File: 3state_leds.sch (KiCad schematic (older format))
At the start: 85 parts, among them U11 74HC595, U12 74HC595, U13 74HC595, U14 74HC595, U15 74HC595

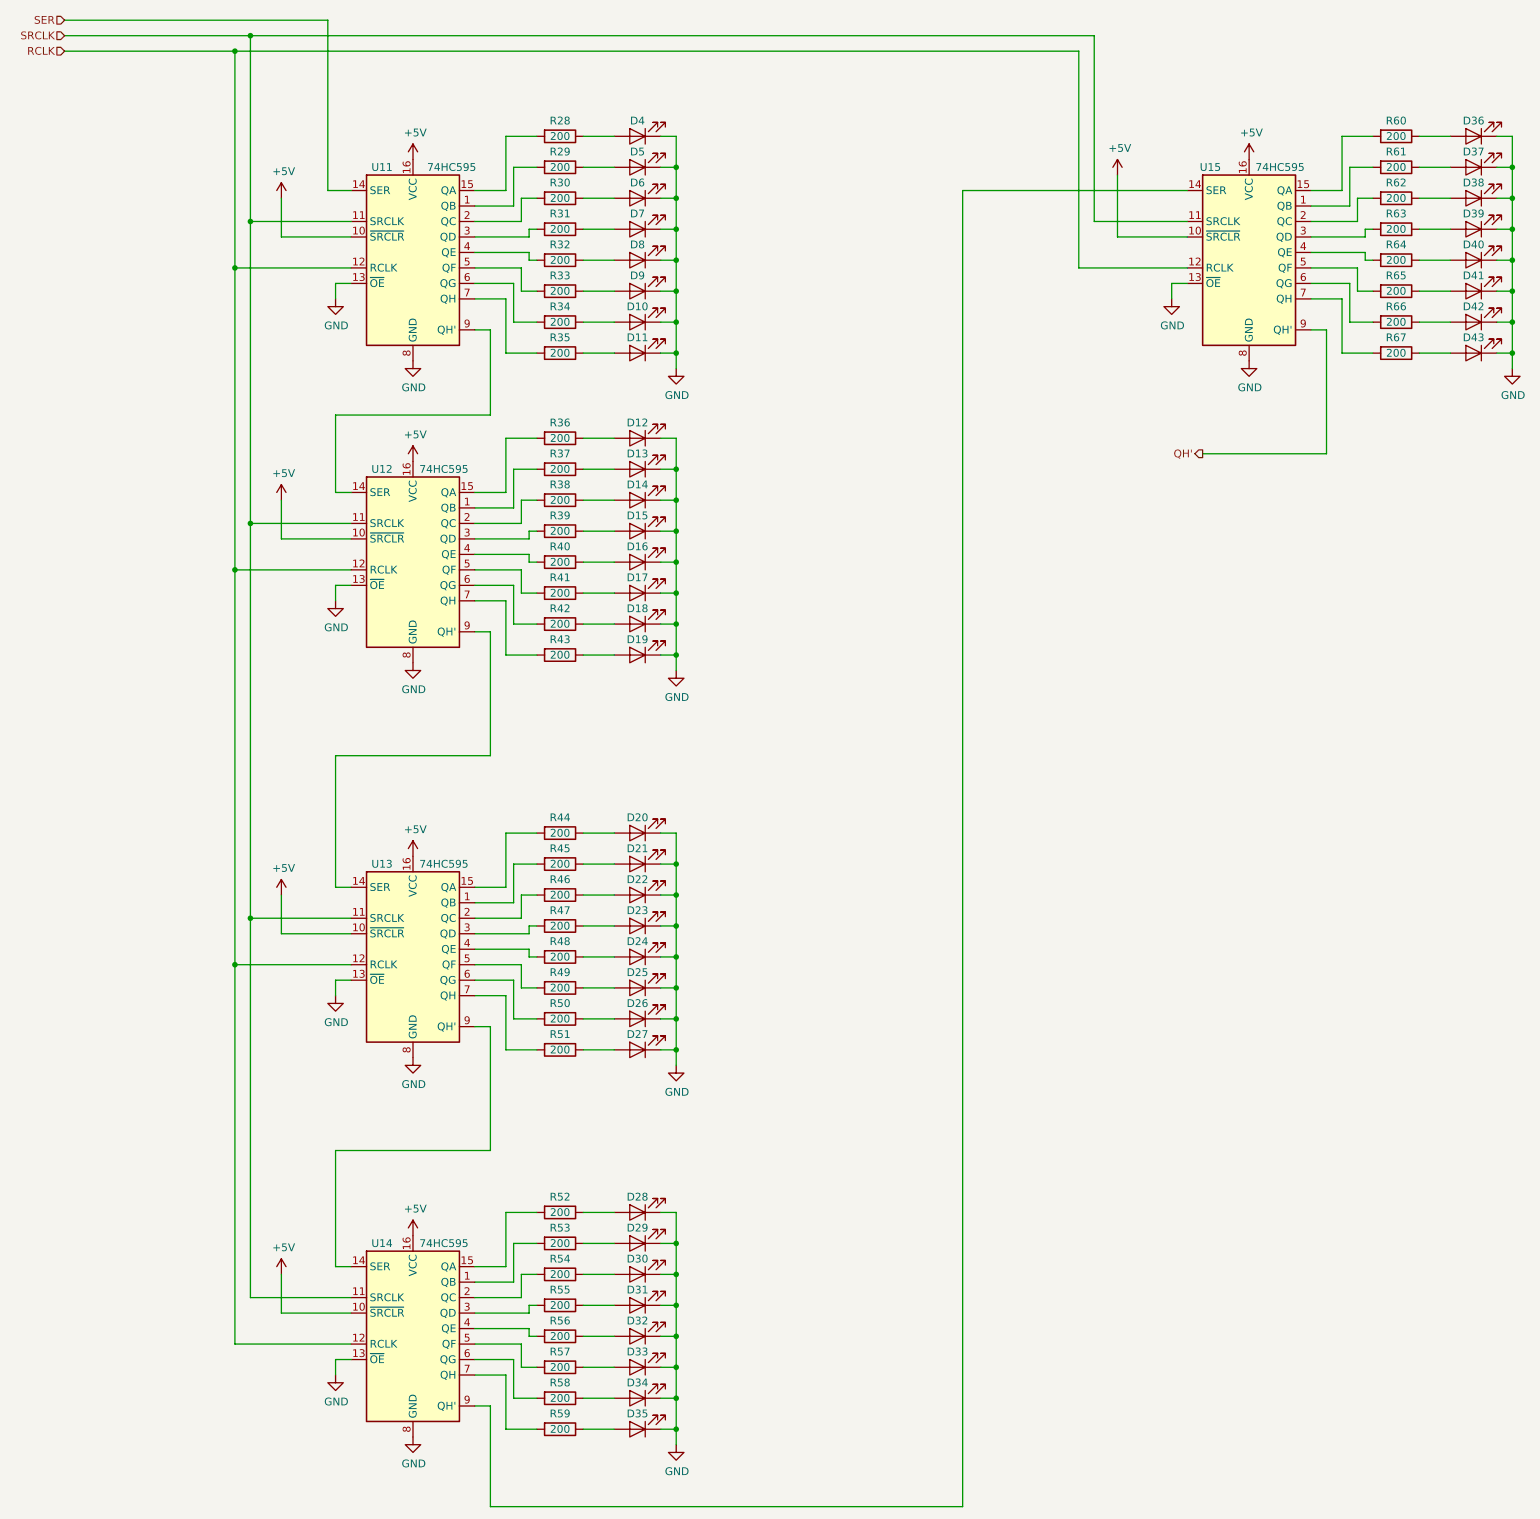
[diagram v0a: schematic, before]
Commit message: reorganized schematic; added reverse polarity protection; start adding footprints
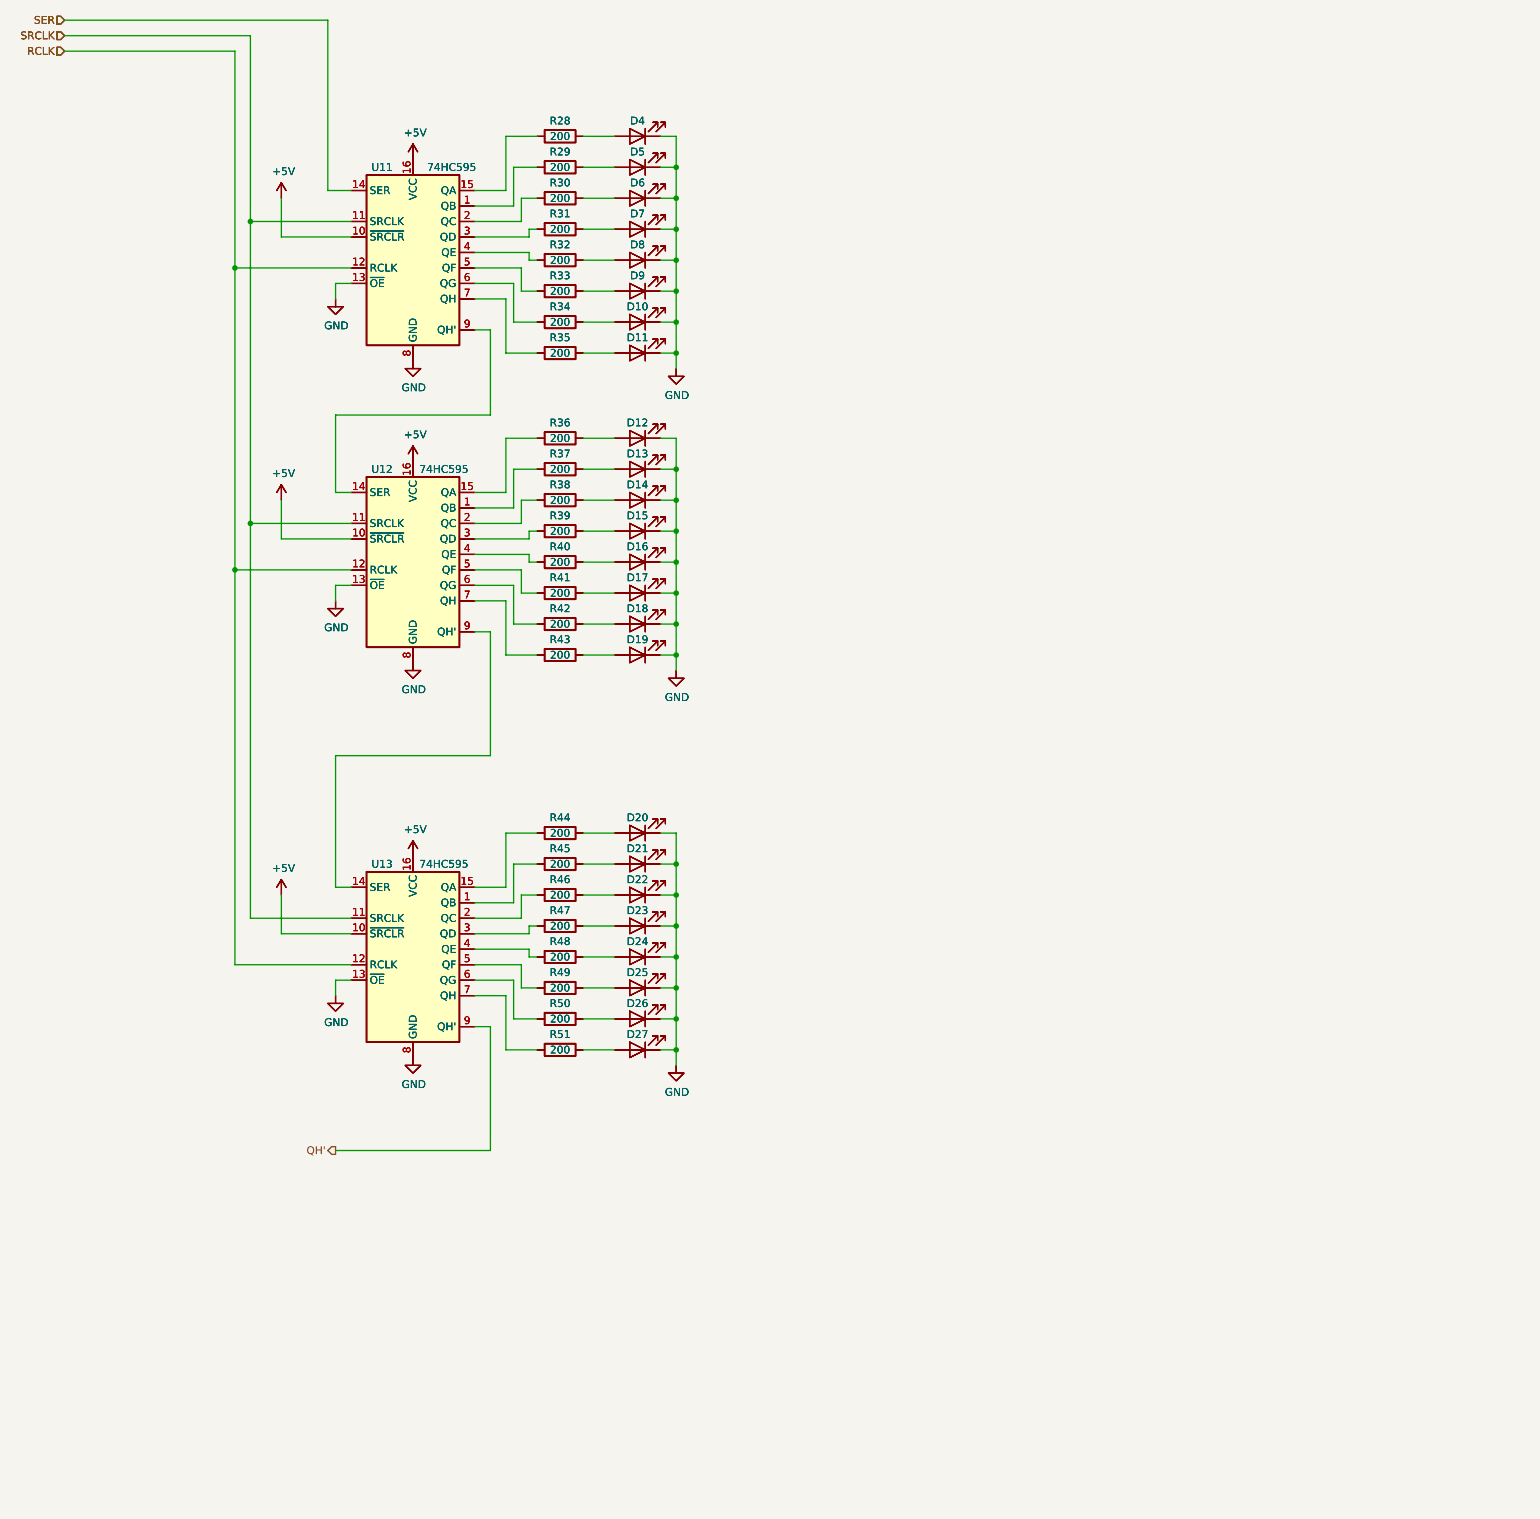
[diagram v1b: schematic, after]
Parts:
- removed D28, D29, D30, D31, D32, D33, D34, D35, D36, D37, D38, D39, D40, D41, D42, D43: LED, symbol Device:LED
- removed R52, R53, R54, R55, R56, R57, R58, R59, R60, R61, R62, R63, R64, R65, R66, R67: 200, symbol Device:R
- removed U14, U15: 74HC595, symbol 74xx:74HC595
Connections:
- net QH': now also U13.9 (QH')

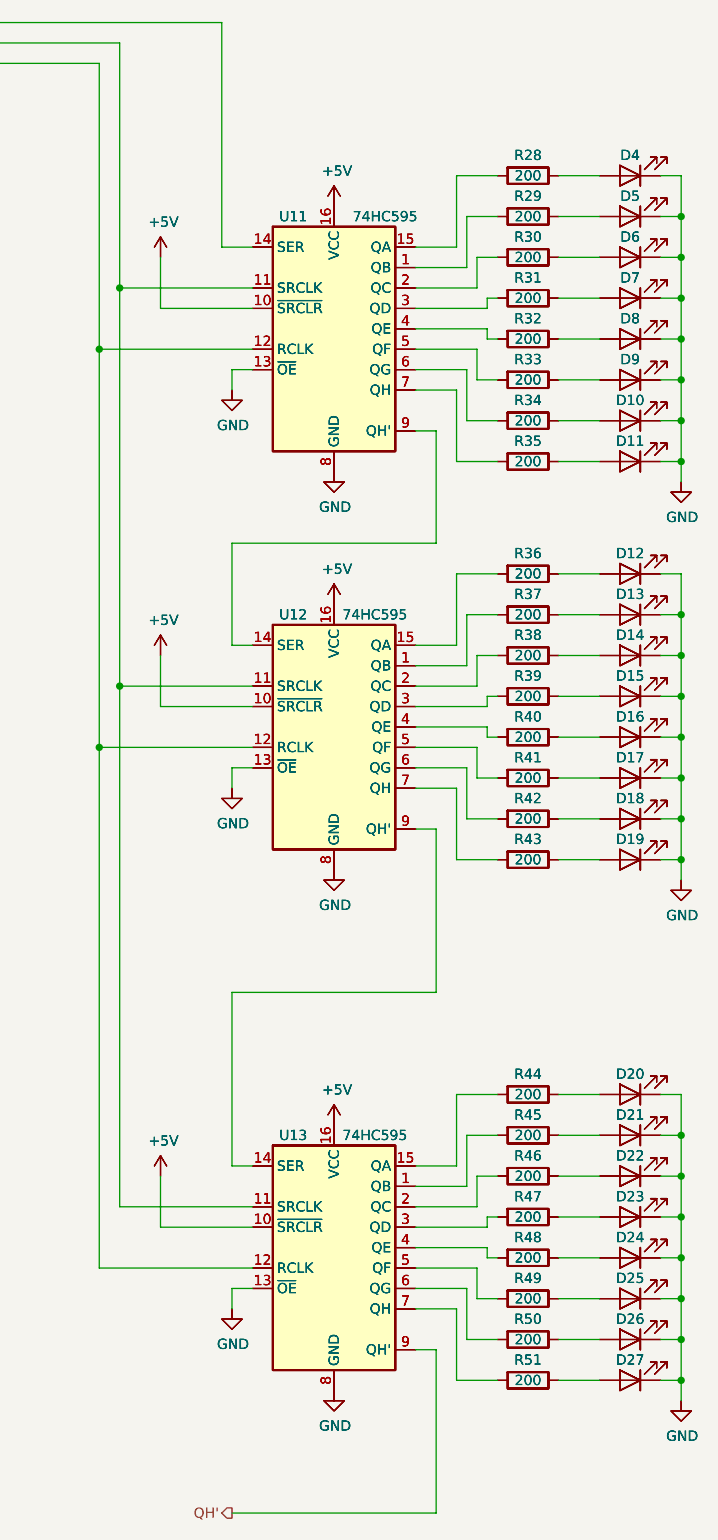
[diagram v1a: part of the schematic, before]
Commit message: footprints; library for 7seg; start pcb layout
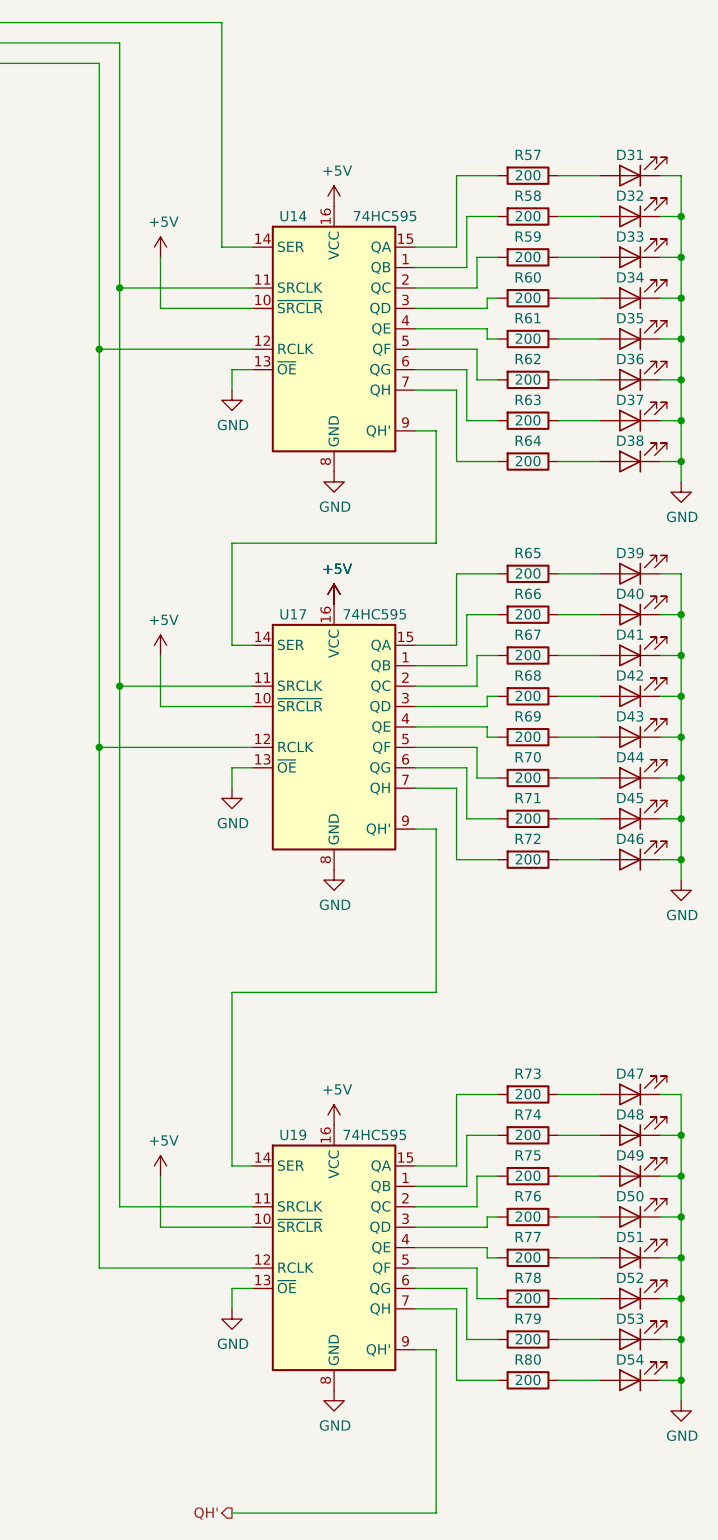
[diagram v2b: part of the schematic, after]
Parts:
- removed D10, D11, D12, D13, D14, D15, D16, D17, D18, D19, D20, D21, D22, D23, D24, D25, D26, D27, D4, D5, D6, D7, D8, D9: LED, symbol Device:LED
- removed R28, R29, R30, R31, R32, R33, R34, R35, R36, R37, R38, R39, R40, R41, R42, R43, R44, R45, R46, R47, R48, R49, R50, R51: 200, symbol Device:R
- removed U11, U12, U13: 74HC595, symbol 74xx:74HC595
- added D31, D32, D33, D34, D35, D36, D37, D38, D39, D40, D41, D42, D43, D44, D45, D46, D47, D48, D49, D50, D51, D52, D53, D54: LED, LED_THT:LED_D3.0mm_Clear, symbol Device:LED
- added R57, R58, R59, R60, R61, R62, R63, R64, R65, R66, R67, R68, R69, R70, R71, R72, R73, R74, R75, R76, R77, R78, R79, R80: 200, Resistor_SMD:R_0603_1608Metric, symbol Device:R
- added U14, U17, U19: 74HC595, Package_SO:SOIC-16_3.9x9.9mm_P1.27mm, symbol 74xx:74HC595
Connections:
- net +5V: now also U14.10 (~SRCLR), U14.16 (VCC), U17.10 (~SRCLR), U17.16 (VCC), U19.10 (~SRCLR), U19.16 (VCC)
- net GND: now also D31.1 (K), D32.1 (K), D33.1 (K), D34.1 (K), D35.1 (K), D36.1 (K), D37.1 (K), D38.1 (K), D39.1 (K), D40.1 (K), D41.1 (K), D42.1 (K), D43.1 (K), D44.1 (K), D45.1 (K), D46.1 (K), D47.1 (K), D48.1 (K), D49.1 (K), D50.1 (K), D51.1 (K), D52.1 (K), D53.1 (K), D54.1 (K), U14.13 (~OE), U14.8 (GND), U17.13 (~OE), U17.8 (GND), U19.13 (~OE), U19.8 (GND)
- net QH': now also U19.9 (QH')
- net RCLK: now also U14.12 (RCLK), U17.12 (RCLK), U19.12 (RCLK)
- net SER: now also U14.14 (SER)
- net SRCLK: now also U14.11 (SRCLK), U17.11 (SRCLK), U19.11 (SRCLK)
- new net: R58.2, U14.1 (QB)
- new net: R57.2, U14.15 (QA)
- new net: R59.2, U14.2 (QC)
- new net: R60.2, U14.3 (QD)
- new net: R61.2, U14.4 (QE)
- new net: R62.2, U14.5 (QF)
- new net: R63.2, U14.6 (QG)
- new net: R64.2, U14.7 (QH)
- new net: U14.9 (QH'), U17.14 (SER)
- new net: R66.2, U17.1 (QB)
- new net: R65.2, U17.15 (QA)
- new net: R67.2, U17.2 (QC)
- new net: R68.2, U17.3 (QD)
- new net: R69.2, U17.4 (QE)
- new net: R70.2, U17.5 (QF)
- new net: R71.2, U17.6 (QG)
- new net: R72.2, U17.7 (QH)
- new net: U17.9 (QH'), U19.14 (SER)
- new net: R74.2, U19.1 (QB)
- new net: R73.2, U19.15 (QA)
- new net: R75.2, U19.2 (QC)
- new net: R76.2, U19.3 (QD)
- new net: R77.2, U19.4 (QE)
- new net: R78.2, U19.5 (QF)
- new net: R79.2, U19.6 (QG)
- new net: R80.2, U19.7 (QH)
- new net: D31.2 (A), R57.1
- new net: D32.2 (A), R58.1
- new net: D33.2 (A), R59.1
- new net: D34.2 (A), R60.1
- new net: D35.2 (A), R61.1
- new net: D36.2 (A), R62.1
- new net: D37.2 (A), R63.1
- new net: D38.2 (A), R64.1
- new net: D39.2 (A), R65.1
- new net: D40.2 (A), R66.1
- new net: D41.2 (A), R67.1
- new net: D42.2 (A), R68.1
- new net: D43.2 (A), R69.1
- new net: D44.2 (A), R70.1
- new net: D45.2 (A), R71.1
- new net: D46.2 (A), R72.1
- new net: D47.2 (A), R73.1
- new net: D48.2 (A), R74.1
- new net: D49.2 (A), R75.1
- new net: D50.2 (A), R76.1
- new net: D51.2 (A), R77.1
- new net: D52.2 (A), R78.1
- new net: D53.2 (A), R79.1
- new net: D54.2 (A), R80.1

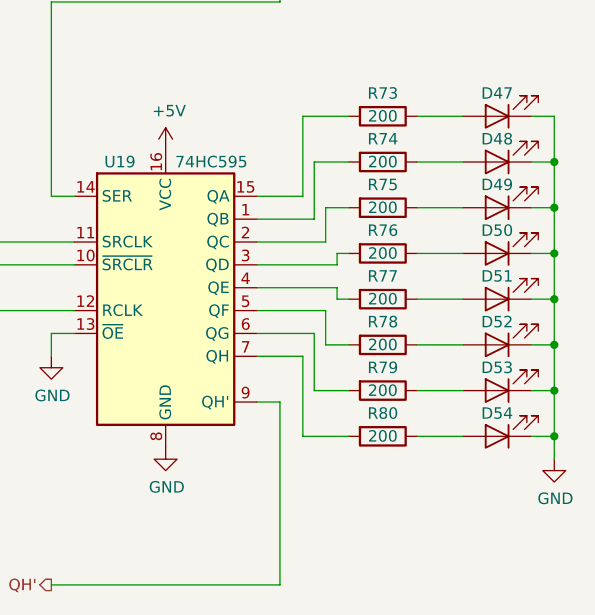
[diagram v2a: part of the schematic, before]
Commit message: remove double elements in 3state leds
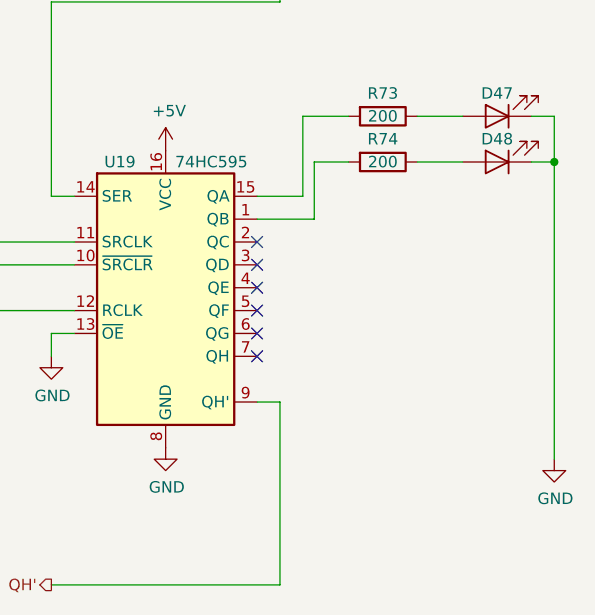
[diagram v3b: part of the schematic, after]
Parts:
- removed D49, D50, D51, D52, D53, D54: LED, LED_THT:LED_D3.0mm_Clear, symbol Device:LED
- removed R75, R76, R77, R78, R79, R80: 200, Resistor_SMD:R_0603_1608Metric, symbol Device:R
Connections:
- no-connect marks 0 -> 6
